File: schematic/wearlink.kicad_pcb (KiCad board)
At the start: 2 copper layers, 24.5 x 21.5 mm, 9 parts, among them J1 JTAG, Q1 MMBT3904, U1 WT51822-0S4AT

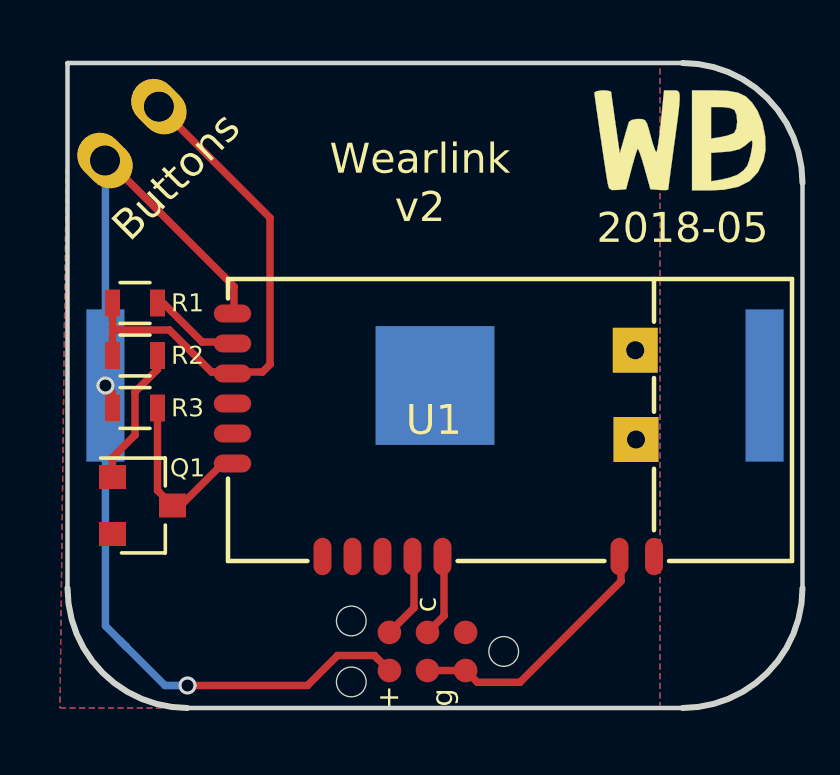
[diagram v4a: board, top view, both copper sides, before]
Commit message: Added via stitching
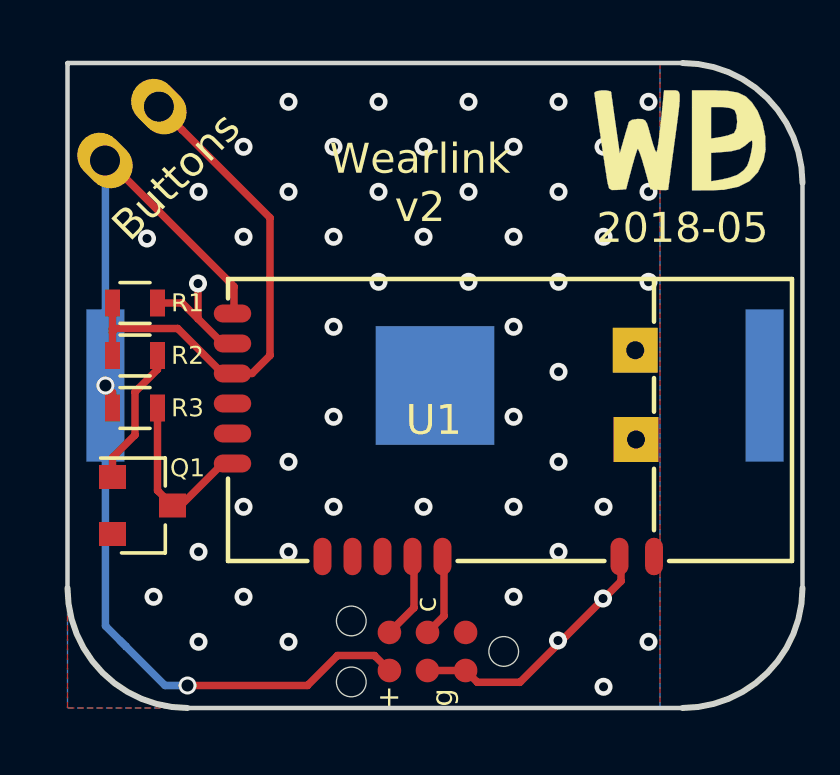
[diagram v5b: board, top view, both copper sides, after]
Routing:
- net GND: track 12.0 -> 13.4 mm, vias 0 -> 51
